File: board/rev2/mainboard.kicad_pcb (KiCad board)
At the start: 4 copper layers, 136.2 x 71.1 mm, 169 parts, among them Q1 WSD40120DN56G, SW1 MS-22D28-G020, SW2 MS-22D28-G020, SW3 MS-22D28-G020, SW4 TS-1088-AR02016, SW5 MS-22D28-G020, U1 TPD6S300A, U10 74VHC161, U11 IS61LV256AL, U12 74AHCT595, U13 IS61LV256AL, U14 74AHCT595, U15 74HCT245, U16 74HCT245, U17 TS3USB30ERSWR, U18 TS3USB30ERSWR, U19 LD1117AG-33-AA3-A-R, U2 TPS62933, U3 TPS259472A, U4 LM5050-1, U5 SiC451, U6 STM32G071CBUx, U7 ESP32-C6-WROOM-1, U8 TLV74311, U9 RP2354B, Y1 ABM8-272-T3

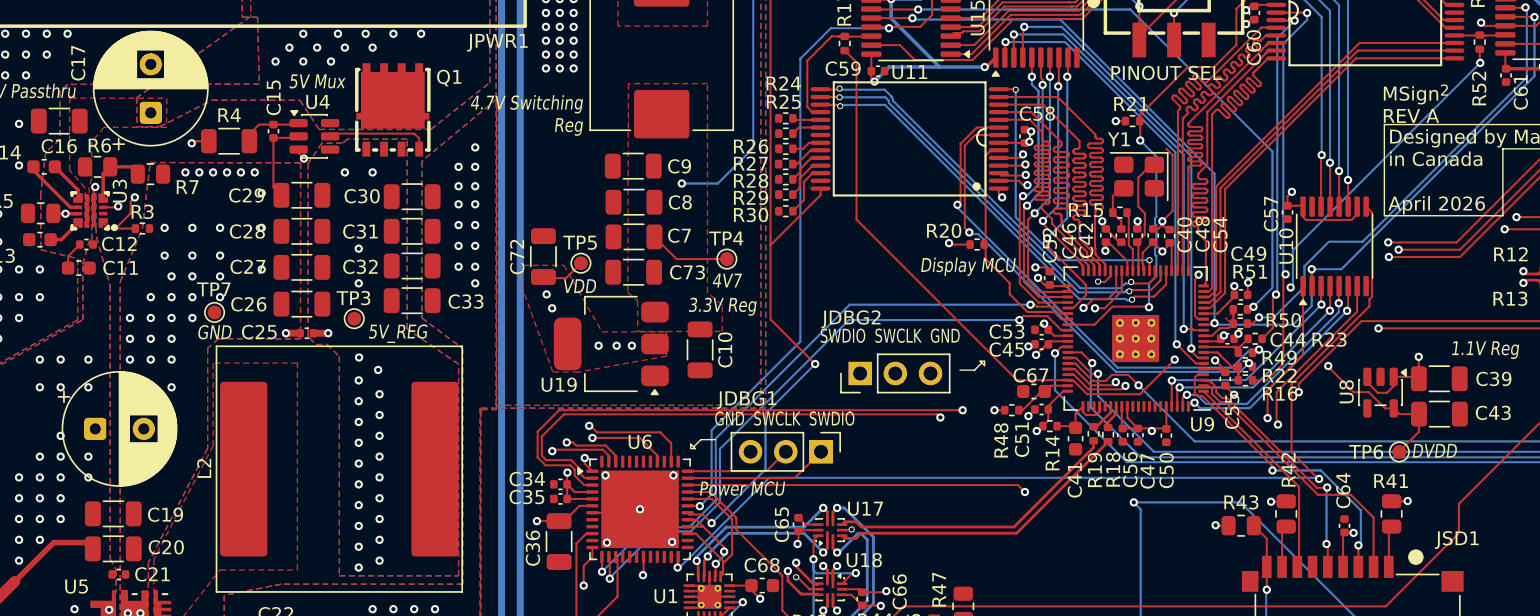
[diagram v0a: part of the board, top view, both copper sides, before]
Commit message: Board REVB - fix 5V mux and add discharge path
also, fix a few routing issues
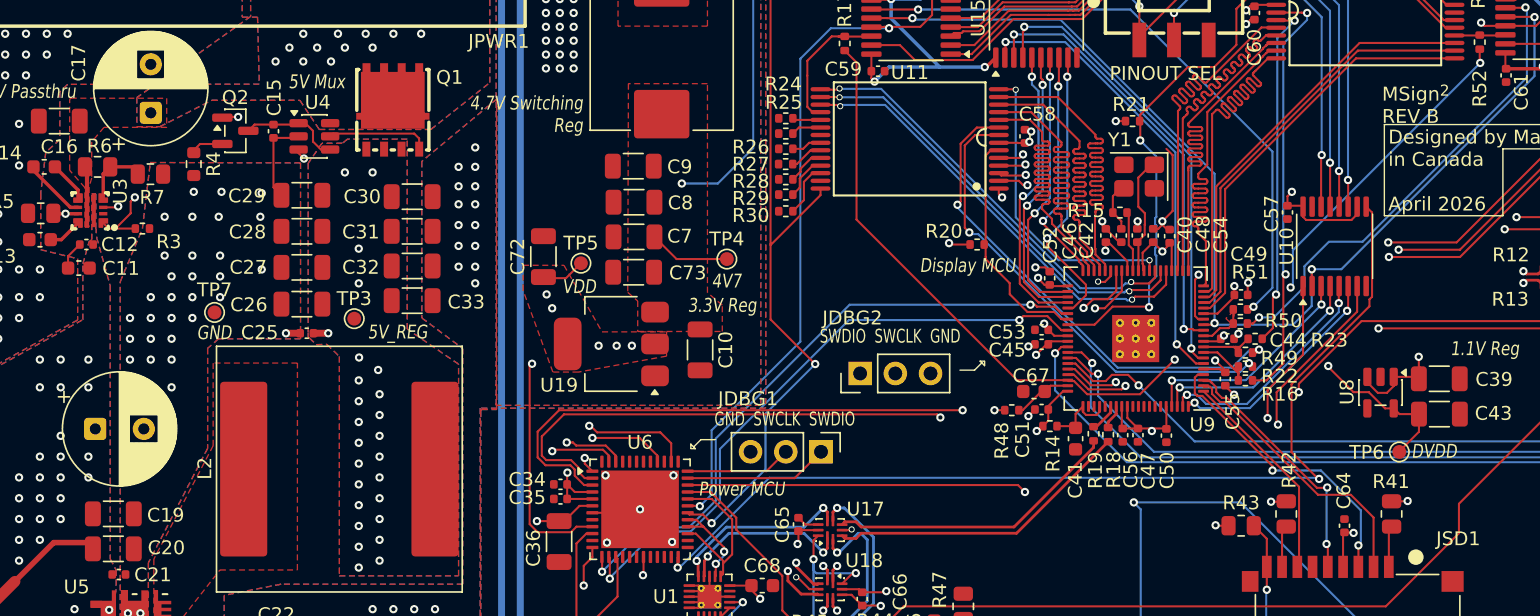
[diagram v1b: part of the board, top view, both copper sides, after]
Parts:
- added Q2: 2N7002, Package_TO_SOT_SMD:SOT-23, F.Cu at (76.6, 114.0)
- R4: footprint Resistor_SMD:R_1206_3216Metric -> Resistor_SMD:R_0603_1608Metric
- SW1, SW2, SW3, SW5: value MS-22D28-G020 -> MS-22D17AG2.5-B
- moved R4 3.04 mm to (73.6, 116.4), turned to -90 degrees
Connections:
- C15 pad 1: Net-(U4-VS) -> /Power/5V_REG
- R4 pad 1: /Power/VBUS -> Net-(Q2-S)
- R4 pad 2: Net-(U4-VS) -> GND
- U4 pad 1: Net-(U4-VS) -> /Power/5V_REG
- U6 pad 9: unconnected-(U6-PF1-Pad9) -> /Power MCU/DISC_5VREG
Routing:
- net /Power MCU/DISC_5VREG: track 0.00 -> 46.3 mm, vias 0 -> 2
- net /Power/VBUS: track 112.3 -> 101.0 mm, vias 35 -> 33
- net /Power/5V_REG: track 0.00 -> 7.37 mm
- net Net-(U4-VS): track 3.60 -> 0.00 mm
- net +5V: track 235.4 -> 238.6 mm
- net Net-(Q2-S): track 0.00 -> 2.42 mm
- net GND: vias 195 -> 191
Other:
- board text added: "MSign^{2} REV B"
- board text removed: "MSign^{2} REV A"
